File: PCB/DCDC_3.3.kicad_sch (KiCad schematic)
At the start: 20 parts, among them Q4 2N7002, U11 LV2842XLVDDCR

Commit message: v0.5 notes
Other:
- note added: "Removed R3 to force always enable"
- note removed: "R3"
- note removed: "Remove R3 to force always enable"
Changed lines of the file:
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@@
-		)
-	)
-	(text "R3"
-		(exclude_from_sim no)
-		(at 121.92 132.08 0)
-		(effects
-			(font
-				(size 1.27 1.27)
-			)
 		)
 	)
@@
 		)
 	)
-	(text "Remove R3 to force always enable"
+	(text "Removed R3 to force always enable"
 		(exclude_from_sim no)
 		(at 113.792 156.972 0)

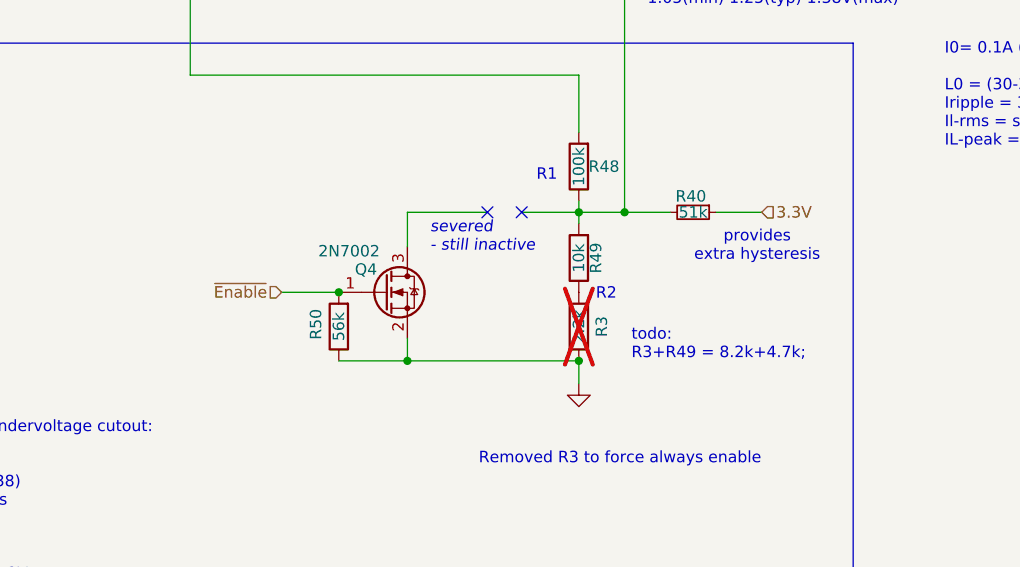
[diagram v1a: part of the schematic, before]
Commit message: tuned start voltage ~11.9V 56k 3.3v hysteresis loop
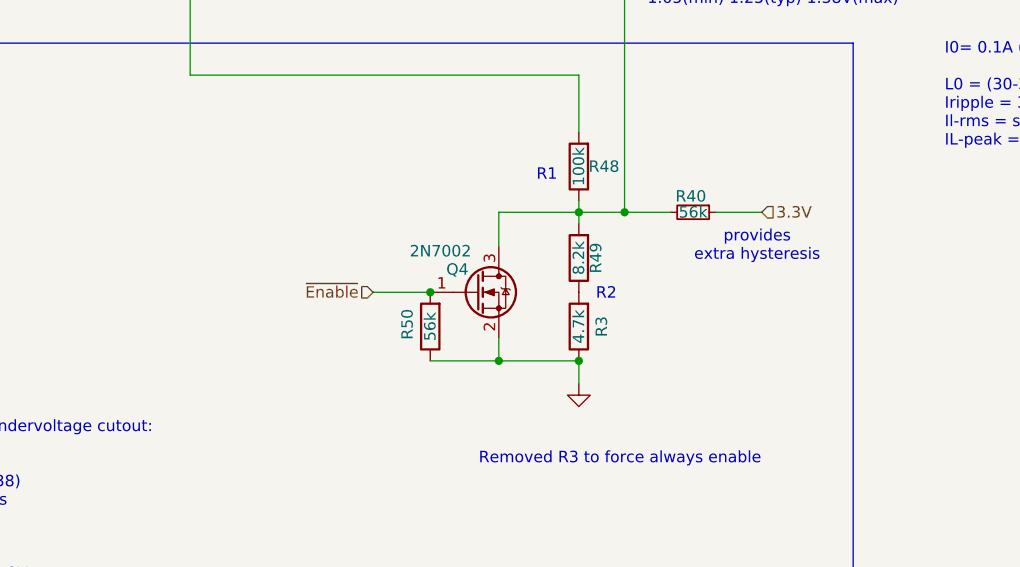
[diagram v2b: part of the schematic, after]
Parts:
- R3: value 2.2k -> 4.7k; LCSC C25879 -> C25900; now fitted
- R40: value 51k -> 56k; LCSC C25794 -> C25796
- R49: value 10k -> 8.2k; LCSC C25744 -> C25924
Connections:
- net at R40.2, R48.1, R49.2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: now also Q4.3 (D)
- no-connect marks 2 -> 0
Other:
- note removed: "severed - still inactive"
- note removed: "todo: R3+R49 = 8.2k+4.7k;"
- moved on the sheet: Q4, R50
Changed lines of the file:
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@@
-		)
-	)
-	(text "severed\n- still inactive"
-		(exclude_from_sim no)
-		(at 92.71 132.334 0)
-		(effects
-			(font
-				(size 1.27 1.27)
-				(italic yes)
-				(color 255 0 255 1)
-			)
-			(justify left)
 		)
 	)
@@
 		)
 	)
-	(text "todo:\nR3+R49 = 8.2k+4.7k;"
-		(exclude_from_sim no)
-		(at 115.062 144.272 0)
-		(effects
-			(font
-				(size 1.27 1.27)
-				(color 255 0 255 1)
-			)
-			(justify left)
-		)
-	)
 	(junction
 		(at 210.82 83.82)
@@
 	)
 	(junction
-		(at 82.55 138.43)
+		(at 92.71 138.43)
 		(diameter 0)
 		(color 0 0 0 0)
@@
 	)
 	(junction
-		(at 90.17 146.05)
+		(at 100.33 146.05)
 		(diameter 0)
 		(color 0 0 0 0)
@@
 		(color 0 0 0 0)
 	)
-	(no_connect
-		(at 102.87 129.54)
-	)
-	(no_connect
-		(at 99.06 129.54)
-	)
 	(wire
 		(pts
@@
 	(wire
 		(pts
-			(xy 102.87 129.54) (xy 109.22 129.54)
-		)
-		(stroke
-			(width 0)
-			(type default)
-		)
-	)
-	(wire
-		(pts
-			(xy 76.2 138.43) (xy 82.55 138.43)
+			(xy 86.36 138.43) (xy 92.71 138.43)
 		)
 		(stroke
@@
 	(wire
 		(pts
-			(xy 90.17 129.54) (xy 90.17 133.35)
+			(xy 100.33 129.54) (xy 100.33 133.35)
 		)
 		(stroke
@@
 	(wire
 		(pts
-			(xy 90.17 143.51) (xy 90.17 146.05)
+			(xy 100.33 143.51) (xy 100.33 146.05)
 		)
 		(stroke
@@
 	(wire
 		(pts
-			(xy 82.55 146.05) (xy 90.17 146.05)
+			(xy 92.71 146.05) (xy 100.33 146.05)
 		)
 		(stroke
@@
 	(wire
 		(pts
-			(xy 90.17 146.05) (xy 109.22 146.05)
+			(xy 100.33 146.05) (xy 109.22 146.05)
 		)
 		(stroke
@@
 	(wire
 		(pts
-			(xy 90.17 129.54) (xy 99.06 129.54)
+			(xy 100.33 129.54) (xy 109.22 129.54)
 		)
 		(stroke
@@
 	(hierarchical_label "~{Enable}"
 		(shape input)
-		(at 76.2 138.43 180)
+		(at 86.36 138.43 180)
 		(effects
 			(font
@@
 			)
 		)
-		(property "Value" "10k"
+		(property "Value" "8.2k"
 			(at 109.22 134.62 90)
 			(effects
@@
 			)
 		)
-		(property "LCSC" "C25744"
+		(property "LCSC" "C25924"
 			(at 111.125 134.62 0)
 			(effects
@@
 		(in_bom yes)
 		(on_board yes)
-		(dnp yes)
+		(dnp no)
 		(property "Reference" "R3"
 			(at 111.76 142.24 90)
@@
 			)
 		)
-		(property "Value" "2.2k"
+		(property "Value" "4.7k"
 			(at 109.22 142.24 90)
 			(effects
@@
 			)
 		)
-		(property "LCSC" "C25879"
+		(property "LCSC" "C25900"
 			(at 106.68 142.875 0)
 			(effects
@@
 	(symbol
 		(lib_id "Device:R")
-		(at 82.55 142.24 180)
+		(at 92.71 142.24 180)
 		(unit 1)
 		(exclude_from_sim no)
@@
 		(dnp no)
 		(property "Reference" "R50"
-			(at 80.01 141.986 90)
+			(at 90.17 141.986 90)
 			(effects
 				(font
@@
 		)
 		(property "Value" "56k"
-			(at 82.55 142.24 90)
+			(at 92.71 142.24 90)
 			(effects
 				(font
@@
 		)
 		(property "Footprint" "Resistor_SMD:R_0402_1005Metric"
-			(at 84.328 142.24 90)
+			(at 94.488 142.24 90)
 			(effects
 				(font
@@
 		)
 		(property "Datasheet" "~"
-			(at 82.55 142.24 0)
-			(effects
-				(font
-					(size 1.27 1.27)
-				)
-				(hide yes)
-			)
-		)
-		(property "Description" ""
-			(at 82.55 142.24 0)
+			(at 92.71 142.24 0)
+			(effects
+				(font
+					(size 1.27 1.27)
+				)
+				(hide yes)
+			)
+		)
+		(property "Description" ""
+			(at 92.71 142.24 0)
 			(effects
 				(font
@@
 		)
 		(property "LCSC" "C25796"
-			(at 84.455 142.24 0)
+			(at 94.615 142.24 0)
 			(effects
 				(font
@@
 			)
 		)
-		(property "Value" "51k"
+		(property "Value" "56k"
 			(at 121.92 129.54 90)
 			(effects
@@
 			)
 		)
-		(property "LCSC" "C25794"
+		(property "LCSC" "C25796"
 			(at 121.92 132.08 0)
 			(effects
@@
 	(symbol
 		(lib_id "Transistor_FET:2N7002")
-		(at 87.63 138.43 0)
+		(at 97.79 138.43 0)
 		(unit 1)
 		(exclude_from_sim no)
@@
 		(dnp no)
 		(property "Reference" "Q4"
-			(at 84.328 135.89 0)
+			(at 94.488 135.89 0)
 			(effects
 				(font
@@
 		)
 		(property "Value" "2N7002"
-			(at 80.264 133.858 0)
+			(at 90.424 133.858 0)
 			(effects
 				(font
@@
 		)
 		(property "Footprint" "Package_TO_SOT_SMD:SOT-23"
-			(at 92.71 140.335 0)
+			(at 102.87 140.335 0)
 			(effects
 				(font
@@
 		)
 		(property "Datasheet" "https://datasheet.lcsc.com/lcsc/2304140030_Jiangsu-Changjing-Electronics-Technology-Co---Ltd--2N7002_C8545.pdf"
-			(at 87.63 138.43 0)
+			(at 97.79 138.43 0)
 			(effects
 				(font
@@
 		)
 		(property "Description" ""
-			(at 87.63 138.43 0)
+			(at 97.79 138.43 0)
 			(effects
 				(font
@@
 		)
 		(property "LCSC" "C8545"
-			(at 87.63 138.43 0)
-			(effects
-				(font
+			(at 97.79 138.43 0)
+			(effects
+				(font
